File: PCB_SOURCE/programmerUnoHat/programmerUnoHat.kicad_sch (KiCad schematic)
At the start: 3 parts, among them J101 Conn_01x06_Pin

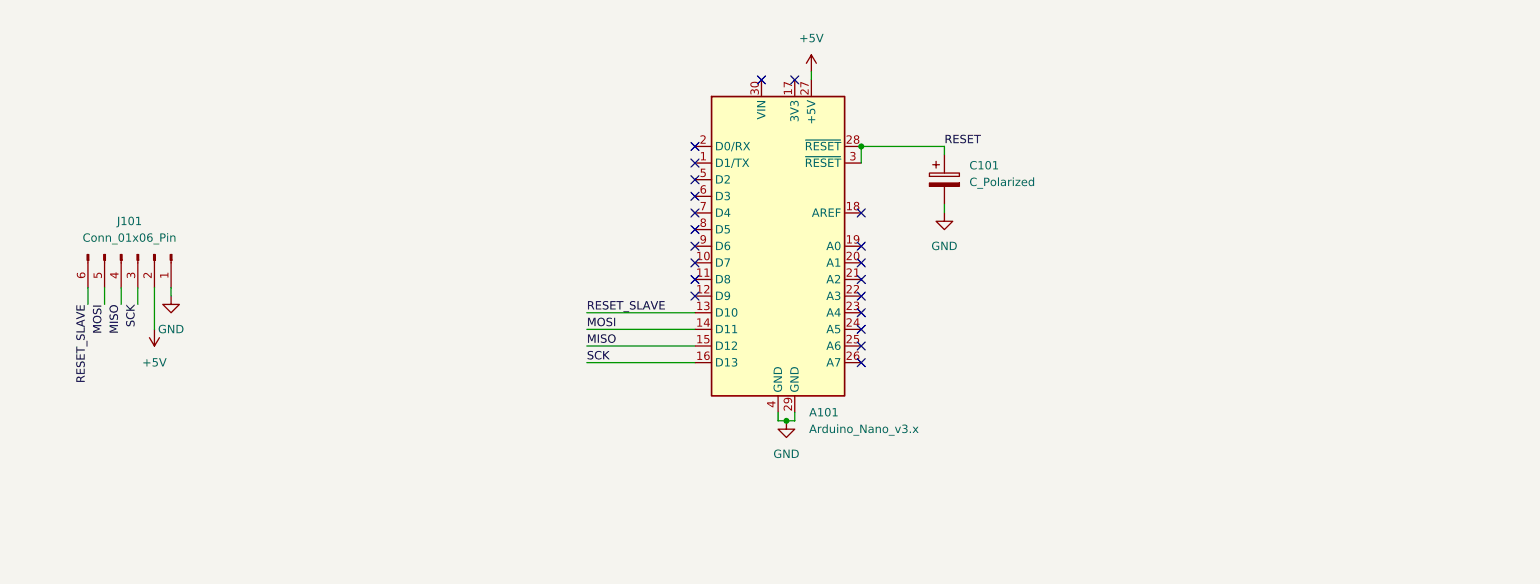
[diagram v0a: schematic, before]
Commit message: added S88 current sense to releases and update OSSD decoder
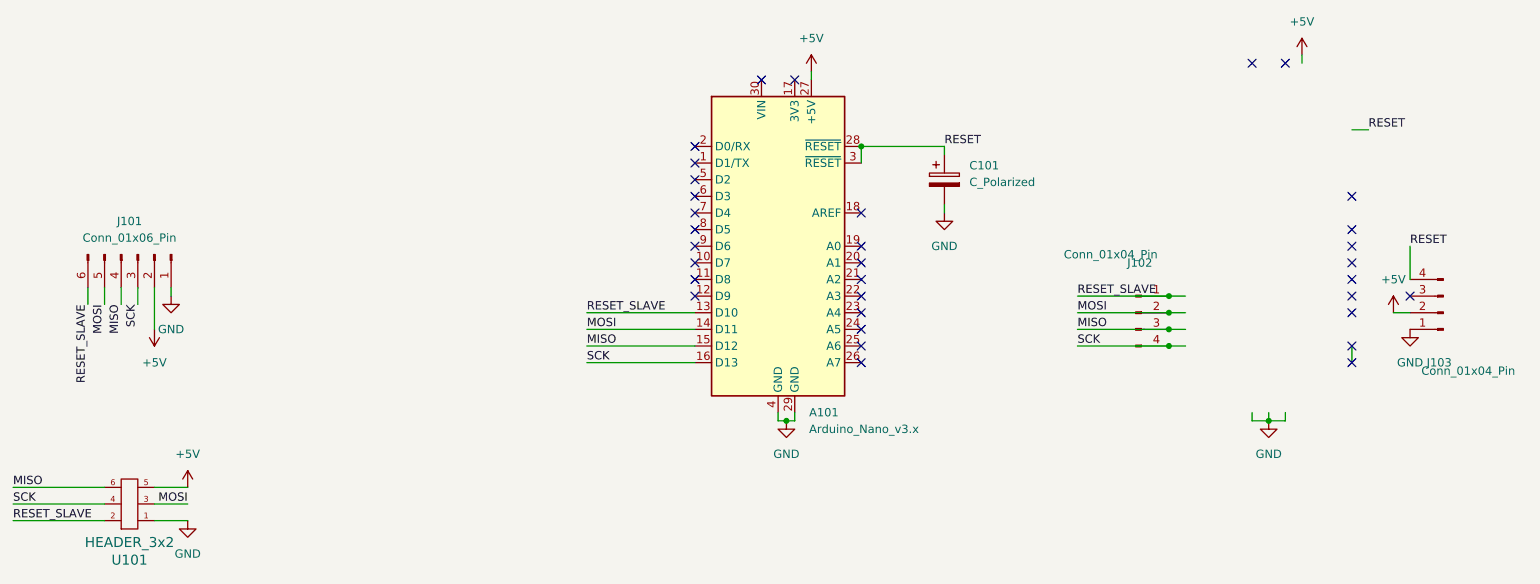
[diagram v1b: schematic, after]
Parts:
- added J102, J103: Conn_01x04_Pin, Connector_PinHeader_2.54mm:PinHeader_1x04_P2.54mm_Vertical, symbol Connector:Conn_01x04_Pin
- added U101: HEADER_3x2, Connector_PinSocket_1.27mm:PinSocket_2x03_P1.27mm_Vertical, symbol servoDriverSMD-rescue:HEADER_3x2-w_connectors
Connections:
- net +5V: now also J103.2 (Pin_2), U101.5
- net GND: now also J103.1 (Pin_1), U101.1
- net MISO: now also J102.3 (Pin_3), U101.6
- net MOSI: now also J102.2 (Pin_2), U101.3
- net RESET: now also J103.4 (Pin_4)
- net RESET_SLAVE: now also J102.1 (Pin_1), U101.2
- net SCK: now also J102.4 (Pin_4), U101.4
- no-connect marks 21 -> 33
